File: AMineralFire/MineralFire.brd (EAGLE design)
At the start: 114.9 x 77 mm, 76 parts, among them IC1 LM358, Q1 20MHz, Q2 20MHz, Q3 2N3906, Q4 2N3906, Q5 2N3906, Q6 2N3906, Q7 2N3906, Q8 2N3906, Q9 2N3906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

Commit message: On Order
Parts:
- moved D2 14.2 mm to (85.1, 53.3)
- moved POWER 6.35 mm to (95.2, 68.6)
- moved R20 5.24 mm to (101.6, 17.8)
- moved R14 5.24 mm to (97.8, 17.8)
- moved R27 5.24 mm to (105.4, 17.8)
- moved U3 5.08 mm to (102.9, 55.9)
- moved C8 2.54 mm to (83.8, 31.8)
- moved D1 2.54 mm to (78.7, 55.9)
- moved MODESW1 2.54 mm to (78.7, 66.0)
- moved PROGSW 2.54 mm to (92.7, 6.35)
- moved Q1 2.54 mm to (64.8, 31.8)
- moved R10 2.54 mm to (69.8, 19.1)
- moved R12 2.54 mm to (69.8, 22.9)
- moved R17 2.54 mm to (78.7, 50.8)
- moved R19 2.54 mm to (41.9, 31.8)
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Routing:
- net GND: track 0.00 -> 461.3 mm, vias 0 -> 1
- net +5V: track 0.00 -> 413.5 mm, vias 0 -> 2
- net +12V: track 0.00 -> 116.0 mm
- net T6: track 0.00 -> 98.1 mm
- net RST: track 0.00 -> 92.7 mm, vias 0 -> 1
- net C-DIG1: track 0.00 -> 78.3 mm
- net T5: track 0.00 -> 77.4 mm
- net MOSI: track 0.00 -> 71.4 mm
- net SCK: track 0.00 -> 70.4 mm
- net N$32: track 0.00 -> 69.5 mm
- net N$20: track 0.00 -> 68.3 mm, vias 0 -> 1
- net TRIGO: track 0.00 -> 68.0 mm, vias 0 -> 1
- net AN-B: track 0.00 -> 68.0 mm
- net AN-A: track 0.00 -> 65.2 mm
- net MISO: track 0.00 -> 63.3 mm
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- added copper zone on layer 16, net N$21
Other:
- board size 114.9 x 77 mm -> 109.9 x 77 mm

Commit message: Fixed up reset
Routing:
- removed copper zone on layer 16, net N$21
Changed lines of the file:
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@@
 <autorouter>
 <pass name="Default">
-<param name="RoutingGrid" value="50mil"/>
+<param name="RoutingGrid" value="0.5mm"/>
 <param name="AutoGrid" value="1"/>
 <param name="Efforts" value="1"/>
 <param name="TopRouterVariant" value="1"/>
 <param name="tpViaShape" value="round"/>
-<param name="PrefDir.1" value="a"/>
+<param name="PrefDir.1" value="-"/>
 <param name="PrefDir.2" value="0"/>
 <param name="PrefDir.3" value="0"/>
@@
 <param name="PrefDir.14" value="0"/>
 <param name="PrefDir.15" value="0"/>
-<param name="PrefDir.16" value="a"/>
+<param name="PrefDir.16" value="|"/>
 <param name="cfVia" value="8"/>
 <param name="cfNonPref" value="5"/>
@@
 <wire x1="36.8046" y1="35.5854" x2="36.83" y2="35.56" width="0.1524" layer="1"/>
 </signal>
-<signal name="N$21">
-<polygon width="0.1524" layer="16">
-<vertex x="0" y="77.47"/>
-<vertex x="110.49" y="77.47"/>
-<vertex x="110.49" y="76.2"/>
-<vertex x="110.49" y="0"/>
-<vertex x="0" y="0"/>
-</polygon>
-</signal>
 </signals>

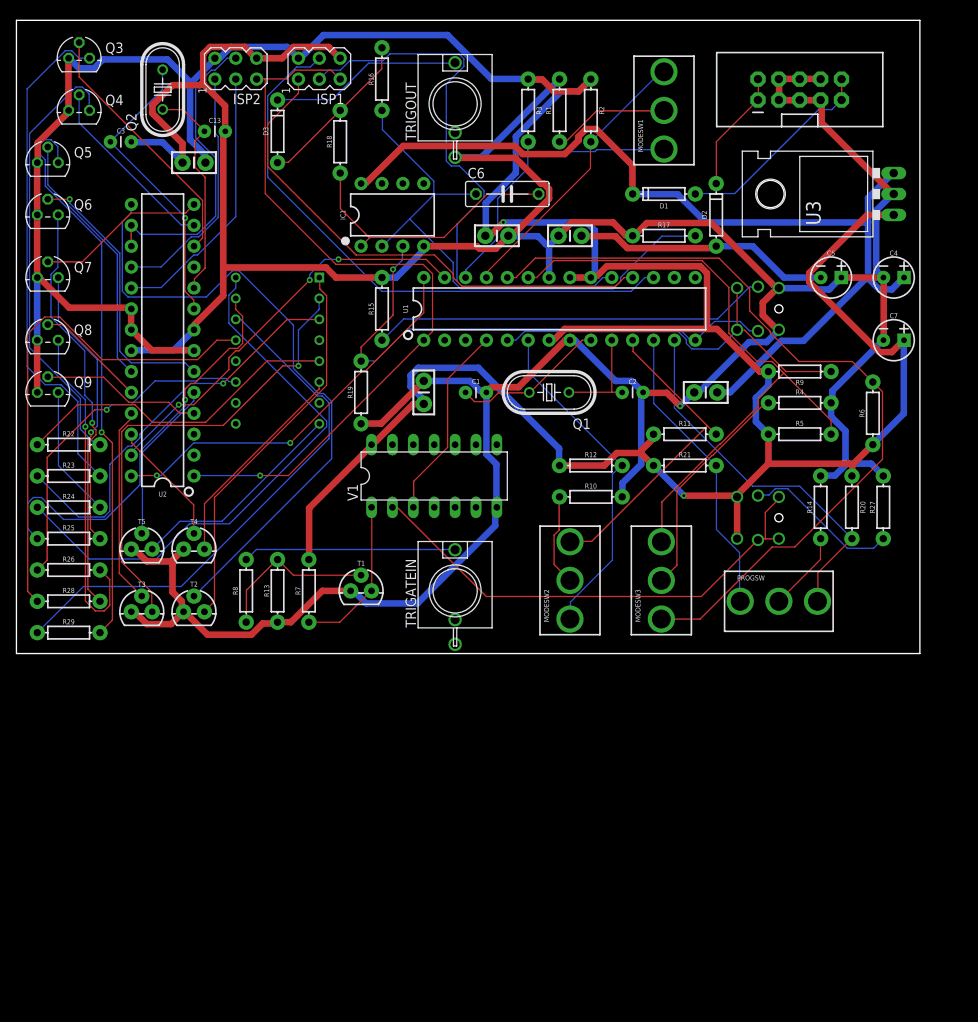
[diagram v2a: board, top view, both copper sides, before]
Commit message: Fixed RST on ISP2 and regulator was wrong way round
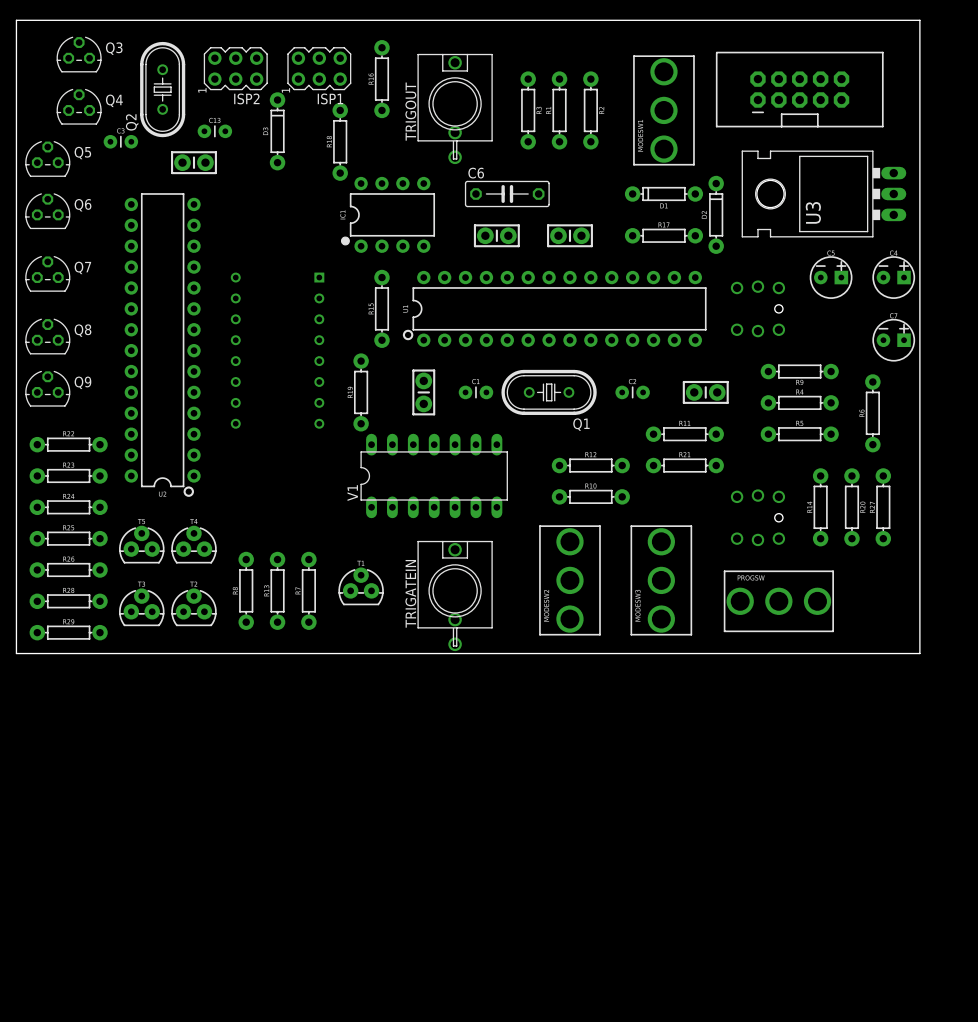
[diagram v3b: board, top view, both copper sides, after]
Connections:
- new net RST2: ISP2.5, U2.1
- net RST: no longer ISP2.5, U2.1
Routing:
- net GND: track 461.3 -> 0.00 mm, vias 1 -> 0
- net +5V: track 413.5 -> 0.00 mm, vias 2 -> 0
- net +12V: track 116.0 -> 0.00 mm
- net T6: track 98.1 -> 0.00 mm
- net RST: track 92.7 -> 0.00 mm, vias 1 -> 0
- net C-DIG1: track 78.3 -> 0.00 mm
- net T5: track 77.4 -> 0.00 mm
- net MOSI: track 71.4 -> 0.00 mm
- net SCK: track 70.4 -> 0.00 mm
- net N$32: track 69.5 -> 0.00 mm
- net N$20: track 68.3 -> 0.00 mm, vias 1 -> 0
- net TRIGO: track 68.0 -> 0.00 mm, vias 1 -> 0
- net AN-B: track 68.0 -> 0.00 mm
- net AN-A: track 65.2 -> 0.00 mm
- net MISO: track 63.3 -> 0.00 mm
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
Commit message: Fixed RST on ISP2 and regulator was wrong way round
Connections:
- net +12V: now also U3.IN; no longer U3.OUT
- net +5V: now also U3.OUT; no longer U3.IN
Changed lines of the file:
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@@
 <contactref element="R20" pad="P$1"/>
 <contactref element="V1" pad="14"/>
-<contactref element="U3" pad="IN"/>
 <contactref element="U2" pad="20"/>
 <contactref element="U2" pad="7"/>
@@
 <contactref element="Q3" pad="3"/>
 <contactref element="Q4" pad="3"/>
-<wire x1="107.93" y1="38.1" x2="106.68" y2="53.34" width="0" layer="19" extent="1-1"/>
+<contactref element="U3" pad="OUT"/>
+<wire x1="107.93" y1="38.1" x2="106.68" y2="58.42" width="0" layer="19" extent="1-1"/>
 <wire x1="104.14" y1="25.4" x2="107.93" y2="38.1" width="0" layer="19" extent="1-1"/>
 <wire x1="101.6" y1="21.59" x2="104.14" y2="25.4" width="0" layer="19" extent="1-1"/>
@@
 <contactref element="C8" pad="1"/>
 <contactref element="IC1" pad="8"/>
-<contactref element="U3" pad="OUT"/>
-<wire x1="107.93" y1="45.72" x2="106.68" y2="58.42" width="0" layer="19" extent="1-1"/>
+<contactref element="U3" pad="IN"/>
+<wire x1="107.93" y1="45.72" x2="106.68" y2="53.34" width="0" layer="19" extent="1-1"/>
 <wire x1="85.217" y1="31.75" x2="107.93" y2="45.72" width="0" layer="19" extent="1-1"/>
 <wire x1="74.93" y1="55.88" x2="85.217" y2="31.75" width="0" layer="19" extent="1-1"/>

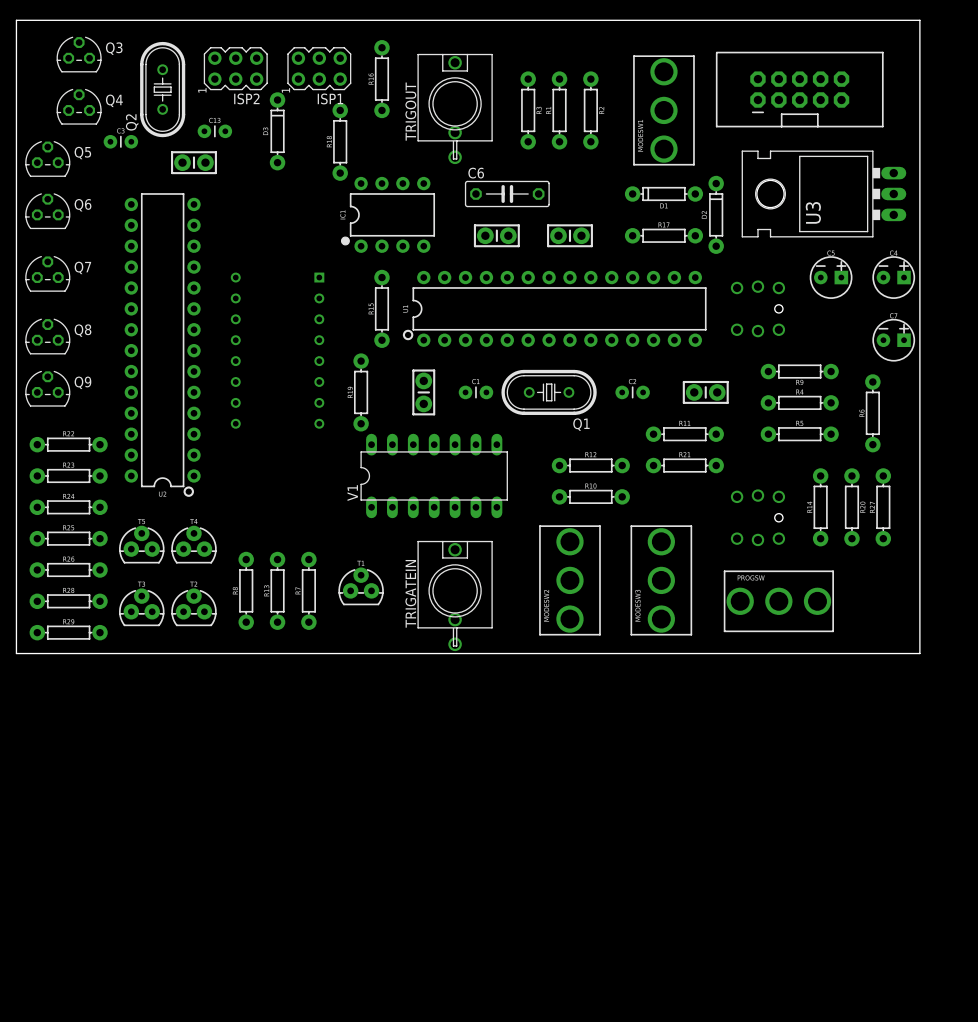
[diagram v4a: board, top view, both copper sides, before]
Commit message: changed push button
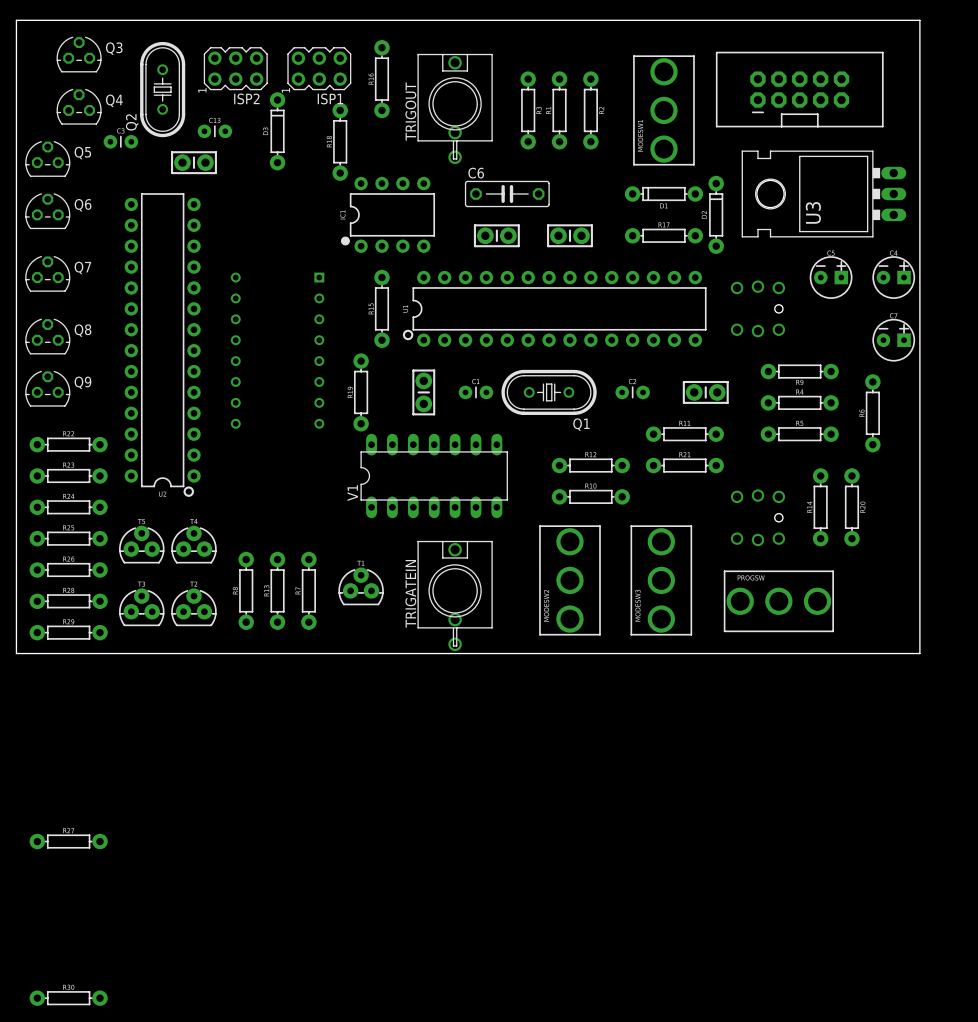
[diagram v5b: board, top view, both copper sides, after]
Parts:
- added R30: 330, SparkFun-Resistors:AXIAL-0.3
- R27: value 150 -> 10k
- moved R27 107.1 mm to (6.35, -22.9), turned to 0 degrees
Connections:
- new net BUTLED: BUT1.A, U1.15
- net +5V: now also R27.P$2; no longer BUT1.1, BUT1.2
- net GND: now also BUT1.3, BUT1.4, R30.P$1; no longer R27.P$2
- net LBUTTON: now also BUT1.1, BUT1.2, R27.P$1; no longer BUT1.3, BUT1.4, BUT1.A
- net N$19: now also R30.P$2; no longer R27.P$1
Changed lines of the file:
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@@
 <element name="BUT" library="INSTRUO" package="PB6149L" value="PB6149L-5" x="90.17" y="41.91" rot="MR0"/>
 <element name="BUT1" library="INSTRUO" package="PB6149L" value="PB6149L-5" x="90.17" y="16.51" rot="MR0"/>
-<element name="R27" library="SparkFun-Resistors" package="AXIAL-0.3" value="150" x="105.41" y="17.78" rot="R90">
-<attribute name="PROD_ID" value="RES-10686" x="105.41" y="17.78" size="1.778" layer="27" rot="R90" display="off"/>
-</element>
 <element name="V1" library="74ttl-din" package="DIL14" value="7432N" x="50.8" y="21.59"/>
 <element name="C6" library="rcl" package="C075-032X103" value="100pf" x="59.69" y="55.88"/>
@@
 <attribute name="PROD_ID" value="RES-12181" x="6.35" y="2.54" size="1.778" layer="27" display="off"/>
 <attribute name="VALUE" value="100" x="6.35" y="2.54" size="1.778" layer="27" display="off"/>
+</element>
+<element name="R27" library="SparkFun-Resistors" package="AXIAL-0.3" value="10k" x="6.35" y="-22.86">
+<attribute name="PROD_ID" value="RES-12183" x="6.35" y="-22.86" size="1.778" layer="27" display="off"/>
+</element>
+<element name="R30" library="SparkFun-Resistors" package="AXIAL-0.3" value="330" x="6.35" y="-41.91">
+<attribute name="PROD_ID" value="RES-8371" x="6.35" y="-41.91" size="1.778" layer="27" display="off"/>
 </element>
 </elements>
@@
 <contactref element="T4" pad="1"/>
 <contactref element="T5" pad="1"/>
-<contactref element="R27" pad="P$2"/>
+<contactref element="BUT1" pad="3"/>
+<contactref element="BUT1" pad="4"/>
+<contactref element="R30" pad="P$1"/>
 <wire x1="97.79" y1="67.31" x2="97.79" y2="69.85" width="0" layer="19" extent="1-1"/>
 <wire x1="95.25" y1="69.85" x2="97.79" y2="69.85" width="0" layer="19" extent="1-1"/>
@@
 <wire x1="99.06" y1="30.48" x2="105.43" y2="38.1" width="0" layer="19" extent="1-1"/>
 <wire x1="97.79" y1="21.59" x2="99.06" y2="30.48" width="0" layer="19" extent="1-1"/>
-<wire x1="105.41" y1="21.59" x2="97.79" y2="21.59" width="0" layer="19" extent="1-1"/>
+<wire x1="92.71" y1="19.05" x2="97.79" y2="21.59" width="0" layer="19" extent="1-1"/>
+<wire x1="92.71" y1="13.97" x2="92.71" y2="19.05" width="0" layer="19" extent="1-1"/>
 <wire x1="82.423" y1="31.75" x2="92.71" y2="39.37" width="0" layer="19" extent="1-1"/>
 <wire x1="76.2" y1="31.75" x2="82.423" y2="31.75" width="0" layer="19" extent="1-1"/>
@@
 <wire x1="21.59" y1="39.37" x2="20.193" y2="59.69" width="0" layer="19" extent="1-1"/>
 <wire x1="13.97" y1="36.83" x2="21.59" y2="39.37" width="0" layer="19" extent="1-1"/>
+<wire x1="2.54" y1="-41.91" x2="13.97" y2="5.08" width="0" layer="19" extent="1-1"/>
 </signal>
 <signal name="RST">
@@
 <contactref element="U2" pad="21"/>
 <contactref element="ISP2" pad="2"/>
-<contactref element="BUT1" pad="1"/>
-<contactref element="BUT1" pad="2"/>
 <contactref element="Q9" pad="3"/>
 <contactref element="Q6" pad="3"/>
@@
 <contactref element="Q4" pad="3"/>
 <contactref element="U3" pad="OUT"/>
+<contactref element="R27" pad="P$2"/>
 <wire x1="107.93" y1="38.1" x2="106.68" y2="58.42" width="0" layer="19" extent="1-1"/>
 <wire x1="104.14" y1="25.4" x2="107.93" y2="38.1" width="0" layer="19" extent="1-1"/>
@@
 <wire x1="91.44" y1="26.67" x2="101.6" y2="21.59" width="0" layer="19" extent="1-1"/>
 <wire x1="91.44" y1="34.29" x2="91.44" y2="26.67" width="0" layer="19" extent="1-1"/>
-<wire x1="87.63" y1="19.05" x2="91.44" y2="26.67" width="0" layer="19" extent="1-1"/>
-<wire x1="87.63" y1="13.97" x2="87.63" y2="19.05" width="0" layer="19" extent="1-1"/>
-<wire x1="77.47" y1="22.86" x2="87.63" y2="19.05" width="0" layer="19" extent="1-1"/>
-<wire x1="77.47" y1="26.67" x2="77.47" y2="22.86" width="0" layer="19" extent="1-1"/>
+<wire x1="77.47" y1="26.67" x2="91.44" y2="26.67" width="0" layer="19" extent="1-1"/>
+<wire x1="77.47" y1="22.86" x2="77.47" y2="26.67" width="0" layer="19" extent="1-1"/>
 <wire x1="66.04" y1="22.86" x2="77.47" y2="22.86" width="0" layer="19" extent="1-1"/>
 <wire x1="64.77" y1="38.1" x2="66.04" y2="22.86" width="0" layer="19" extent="1-1"/>
@@
 <wire x1="34.29" y1="72.39" x2="24.13" y2="72.39" width="0" layer="19" extent="1-1"/>
 <wire x1="22.987" y1="59.69" x2="24.13" y2="72.39" width="0" layer="19" extent="1-1"/>
+<wire x1="10.16" y1="-22.86" x2="35.56" y2="11.43" width="0" layer="19" extent="1-1"/>
 </signal>
 <signal name="MISO">
@@
 <signal name="LBUTTON">
 <contactref element="V1" pad="2"/>
-<contactref element="BUT1" pad="3"/>
-<contactref element="BUT1" pad="4"/>
-<contactref element="BUT1" pad="A"/>
-<wire x1="92.71" y1="13.97" x2="92.71" y2="19.05" width="0" layer="19" extent="1-1"/>
-<wire x1="90.17" y1="13.81" x2="92.71" y2="13.97" width="0" layer="19" extent="1-1"/>
-<wire x1="45.72" y1="17.78" x2="90.17" y2="13.81" width="0" layer="19" extent="1-1"/>
+<contactref element="R27" pad="P$1"/>
+<contactref element="BUT1" pad="2"/>
+<contactref element="BUT1" pad="1"/>
+<wire x1="87.63" y1="13.97" x2="87.63" y2="19.05" width="0" layer="19" extent="1-1"/>
+<wire x1="45.72" y1="17.78" x2="87.63" y2="19.05" width="0" layer="19" extent="1-1"/>
+<wire x1="2.54" y1="-22.86" x2="45.72" y2="17.78" width="0" layer="19" extent="1-1"/>
 </signal>
 <signal name="N$7">
@@
 <wire x1="21.59" y1="14.605" x2="13.97" y2="26.67" width="0" layer="19" extent="1-1"/>
 </signal>
-<signal name="N$19">
-<contactref element="BUT1" pad="K"/>
-<contactref element="R27" pad="P$1"/>
-<wire x1="90.17" y1="19.21" x2="105.41" y2="13.97" width="0" layer="19" extent="1-1"/>
-</signal>
 <signal name="D1">
 <contactref element="T2" pad="3"/>
@@
 <wire x1="21.59" y1="21.59" x2="29.21" y2="69.85" width="0" layer="19" extent="1-1"/>
 </signal>
+<signal name="N$19">
+<contactref element="BUT1" pad="K"/>
+<contactref element="R30" pad="P$2"/>
+<wire x1="10.16" y1="-41.91" x2="90.17" y2="19.21" width="0" layer="19" extent="1-1"/>
+</signal>
+<signal name="BUTLED">
+<contactref element="U1" pad="15"/>
+<contactref element="BUT1" pad="A"/>
+<wire x1="90.17" y1="13.81" x2="82.55" y2="45.72" width="0" layer="19" extent="1-1"/>
+</signal>
 </signals>

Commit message: updated to and gate
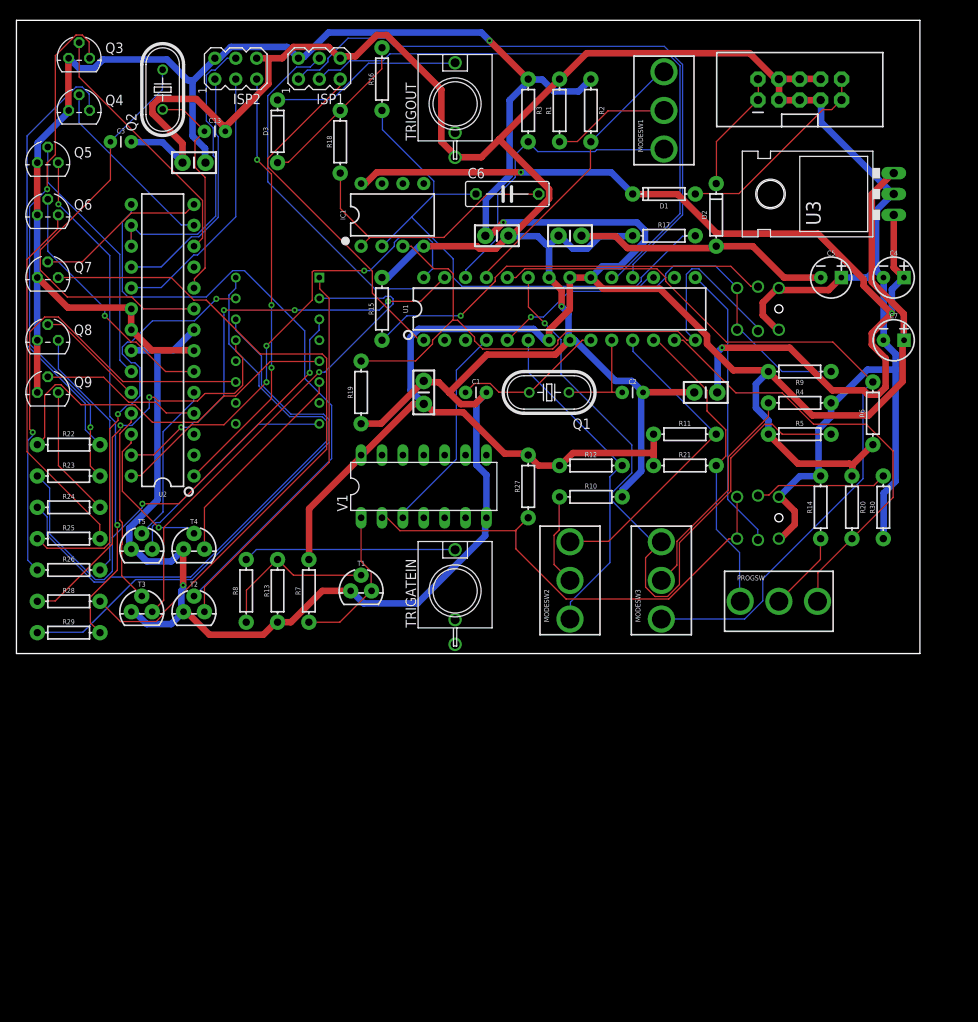
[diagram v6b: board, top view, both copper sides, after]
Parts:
- V1: value 7432N -> 7409N
- moved R30 115.7 mm to (105.4, 17.8), turned to 90 degrees
- moved R27 70.6 mm to (62.2, 20.3), turned to 90 degrees
- moved V1 1.80 mm to (49.5, 20.3)
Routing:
- net GND: track 0.00 -> 496.6 mm, vias 0 -> 2
- net +5V: track 0.00 -> 400.9 mm, vias 0 -> 2
- net +12V: track 0.00 -> 124.8 mm, vias 0 -> 3
- net T6: track 0.00 -> 96.3 mm
- net T5: track 0.00 -> 85.3 mm, vias 0 -> 1
- net N$16: track 0.00 -> 85.1 mm
- net TRIGO: track 0.00 -> 80.3 mm
- net MISO: track 0.00 -> 78.8 mm
- net C-DIG1: track 0.00 -> 78.4 mm
- net SCK: track 0.00 -> 75.2 mm
- net AN-B: track 0.00 -> 74.8 mm
- net MOSI: track 0.00 -> 71.5 mm
- net N$32: track 0.00 -> 69.1 mm
- net AN-A: track 0.00 -> 67.1 mm
- net N$11: track 0.00 -> 63.5 mm, vias 0 -> 2
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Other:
- board text added: "Board_v0.21"
- board text removed: "Board_v0.2"
